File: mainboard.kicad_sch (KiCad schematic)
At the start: 30 parts, among them J1 terminal_led-strip, J2 header_rotary-encoder, J3 AudioJack2, J4 header_rpi, J5 power_input, Q1 IRF9540N, SW1 power_switch, U2 MSGEQ7, U3 OPA197xDBV, U4 logic-level-converter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

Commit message: finish schematic
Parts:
- removed R_led-strip_1, R_led-strip_2: 220, Resistor_SMD:R_0603_1608Metric_Pad0.98x0.95mm_HandSolder, symbol Device:R
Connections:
- net at R3.2, R5.1: now also U6.6 (4)
- net at U4.11 (HV2): now also J1.5 (Pin_5)
- net at U4.12 (HV1): now also J1.2 (Pin_2)
- net rotary_sw: now reaches J2.3 (Pin_3)
- net rotary_sw: now also U6.28 (1)
- net rotary_dt: now reaches J2.4 (Pin_4)
- net rotary_dt: now also U6.27 (2)
- net rotary_clk: now reaches J2.5 (Pin_5)
- net rotary_clk: now also U6.26 (3)
- net at J4.2 (Pin_2), SCL_pullup.2: now also U6.22 (RX)
- net at J4.3 (Pin_3), SDA_pullup.2: now also U6.21 (TX)
- net esp_led-strip_back: now reaches U6.12 (9)
- net esp_led-strip_back: now also U4.2 (LV2)
- net at U6.24 (10): now also U5.1 (LV1)
- net esp_msgeq7-strobe: now reaches U6.7 (5)
- net esp_msgeq7-strobe: now also U4.5 (LV3)
- net esp_msgeq7-reset: now reaches U6.8 (6)
- net esp_msgeq7-reset: now also U4.6 (LV4)
- net esp_led-strip_front: now reaches U6.9 (7)
- net esp_led-strip_front: now also U4.1 (LV1)
- net msgeq7_out renamed msgeq7-out
- net msgeq7_reset renamed msgeq7-reset
- net msgeq7_strobe renamed msgeq7-strobe
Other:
- moved on the sheet: U5

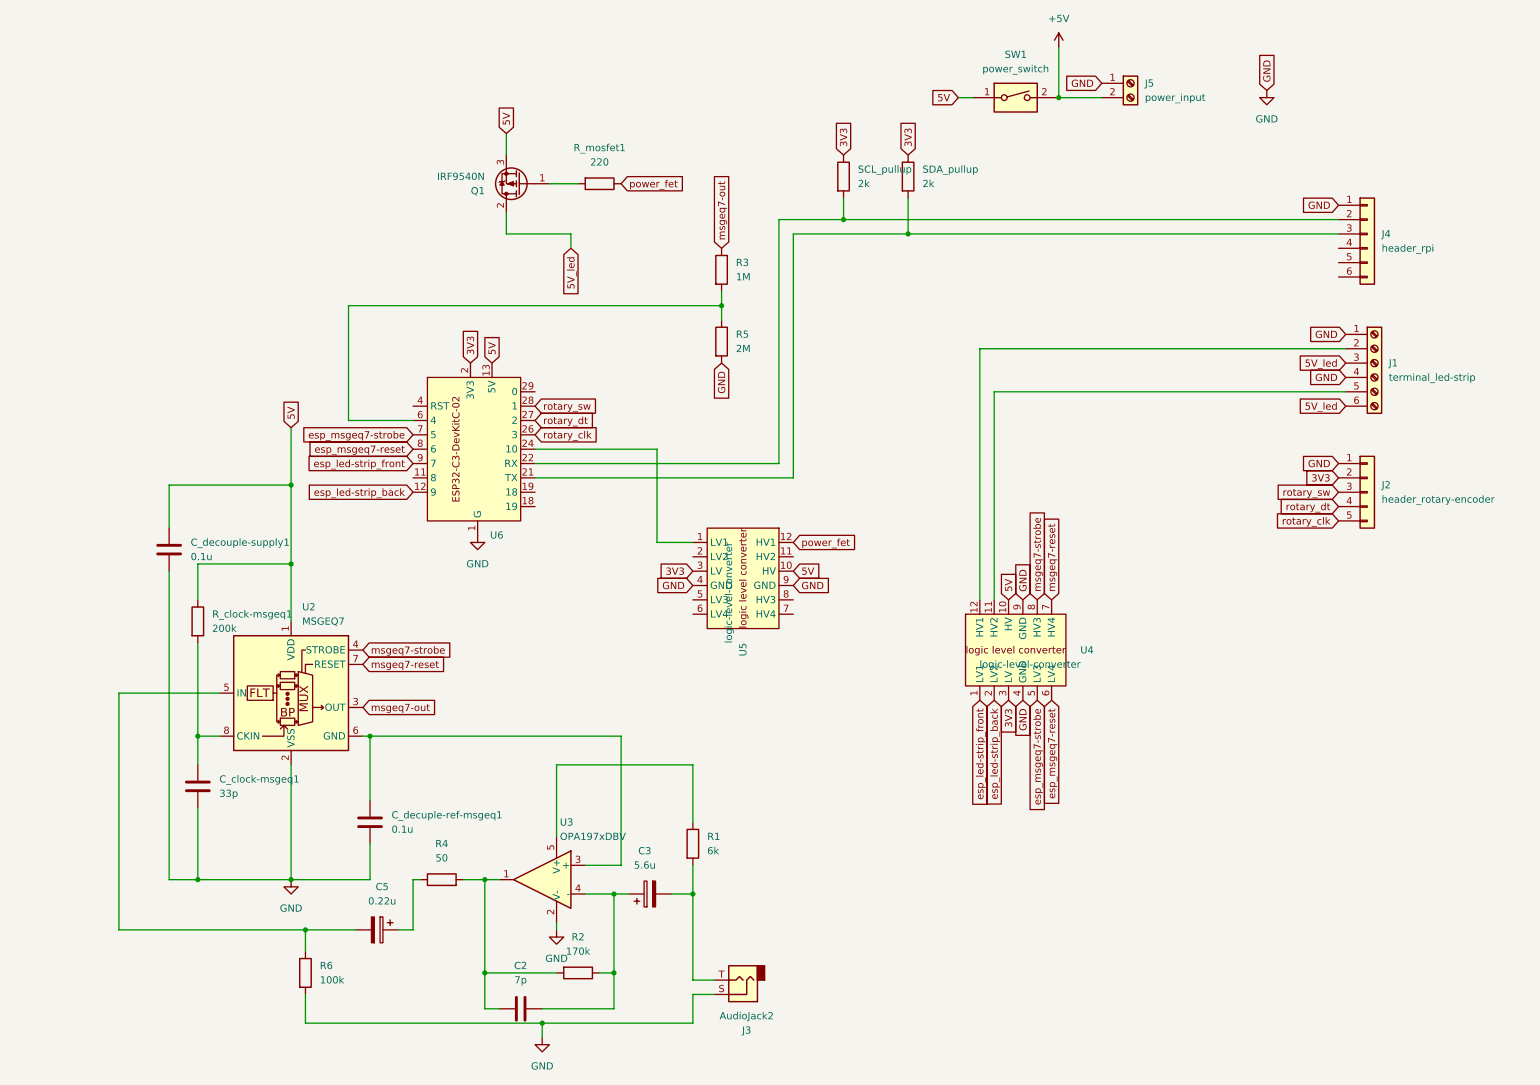
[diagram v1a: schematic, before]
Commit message: move i2c pins
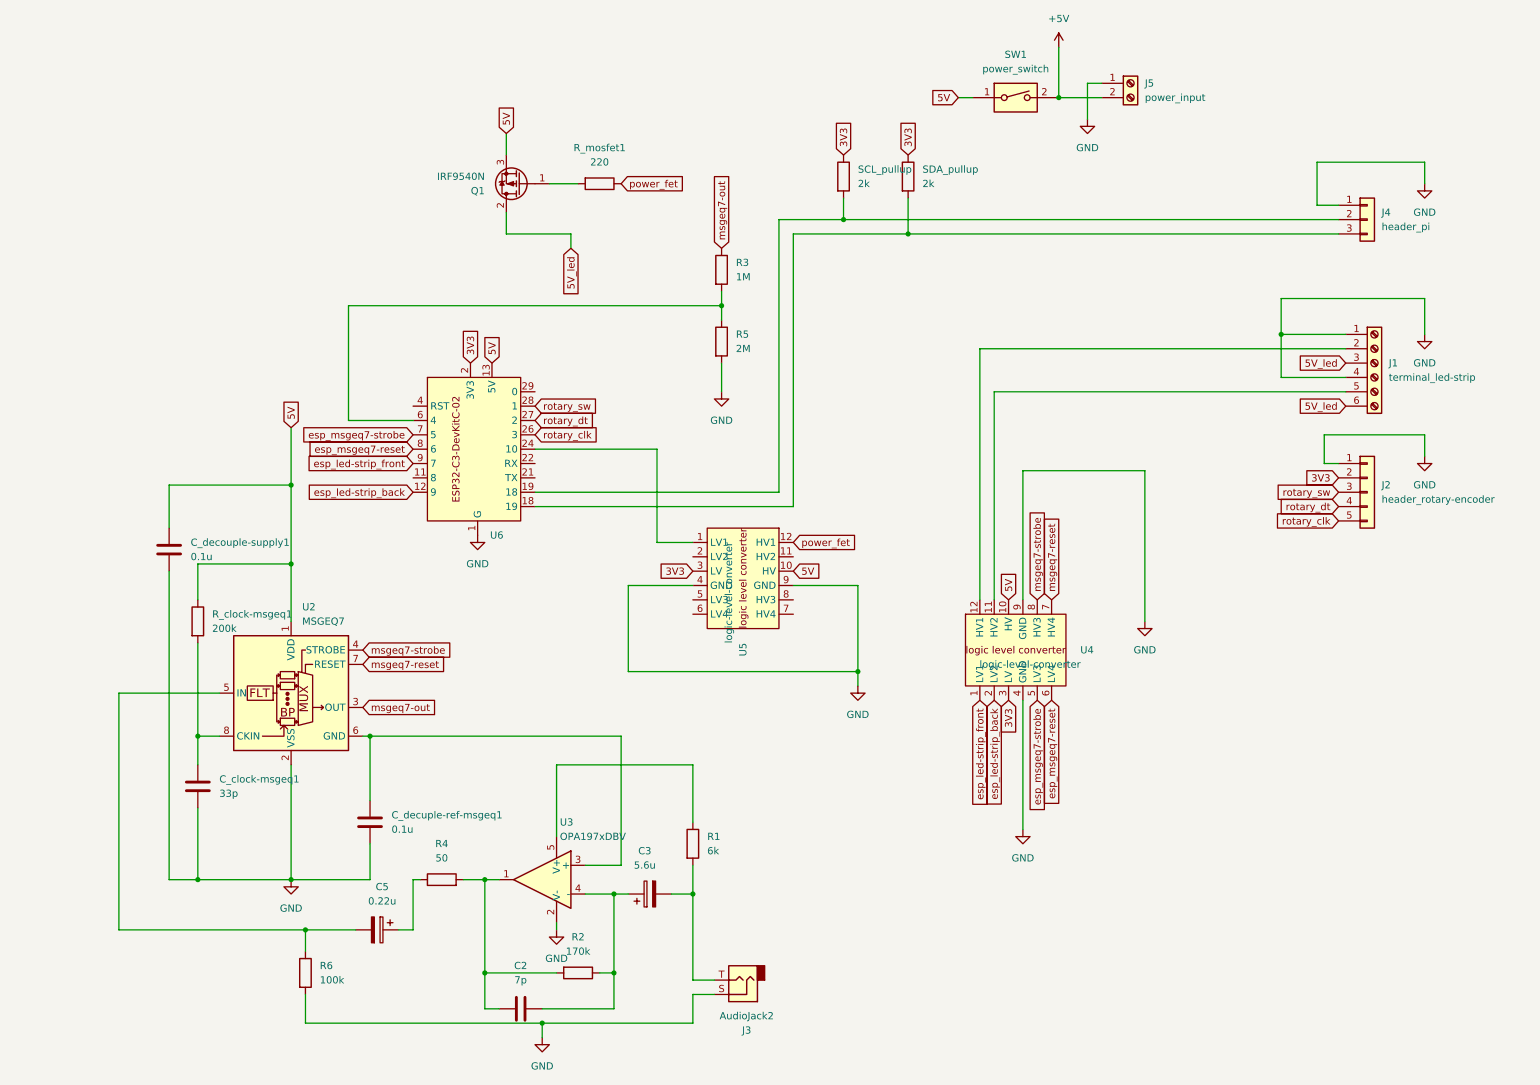
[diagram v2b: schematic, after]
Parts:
- removed J4: header_rpi, Connector_PinHeader_2.54mm:PinHeader_1x06_P2.54mm_Vertical, symbol Connector_Generic:Conn_01x06
- added J4: header_pi, symbol Connector_Generic:Conn_01x03
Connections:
- net GND: now also J4.1 (Pin_1)
- net at SCL_pullup.2: now also U6.19 (18), J4.2 (Pin_2); no longer U6.22 (RX)
- net at SDA_pullup.2: now also U6.18 (19), J4.3 (Pin_3); no longer U6.21 (TX)

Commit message: add loudness control
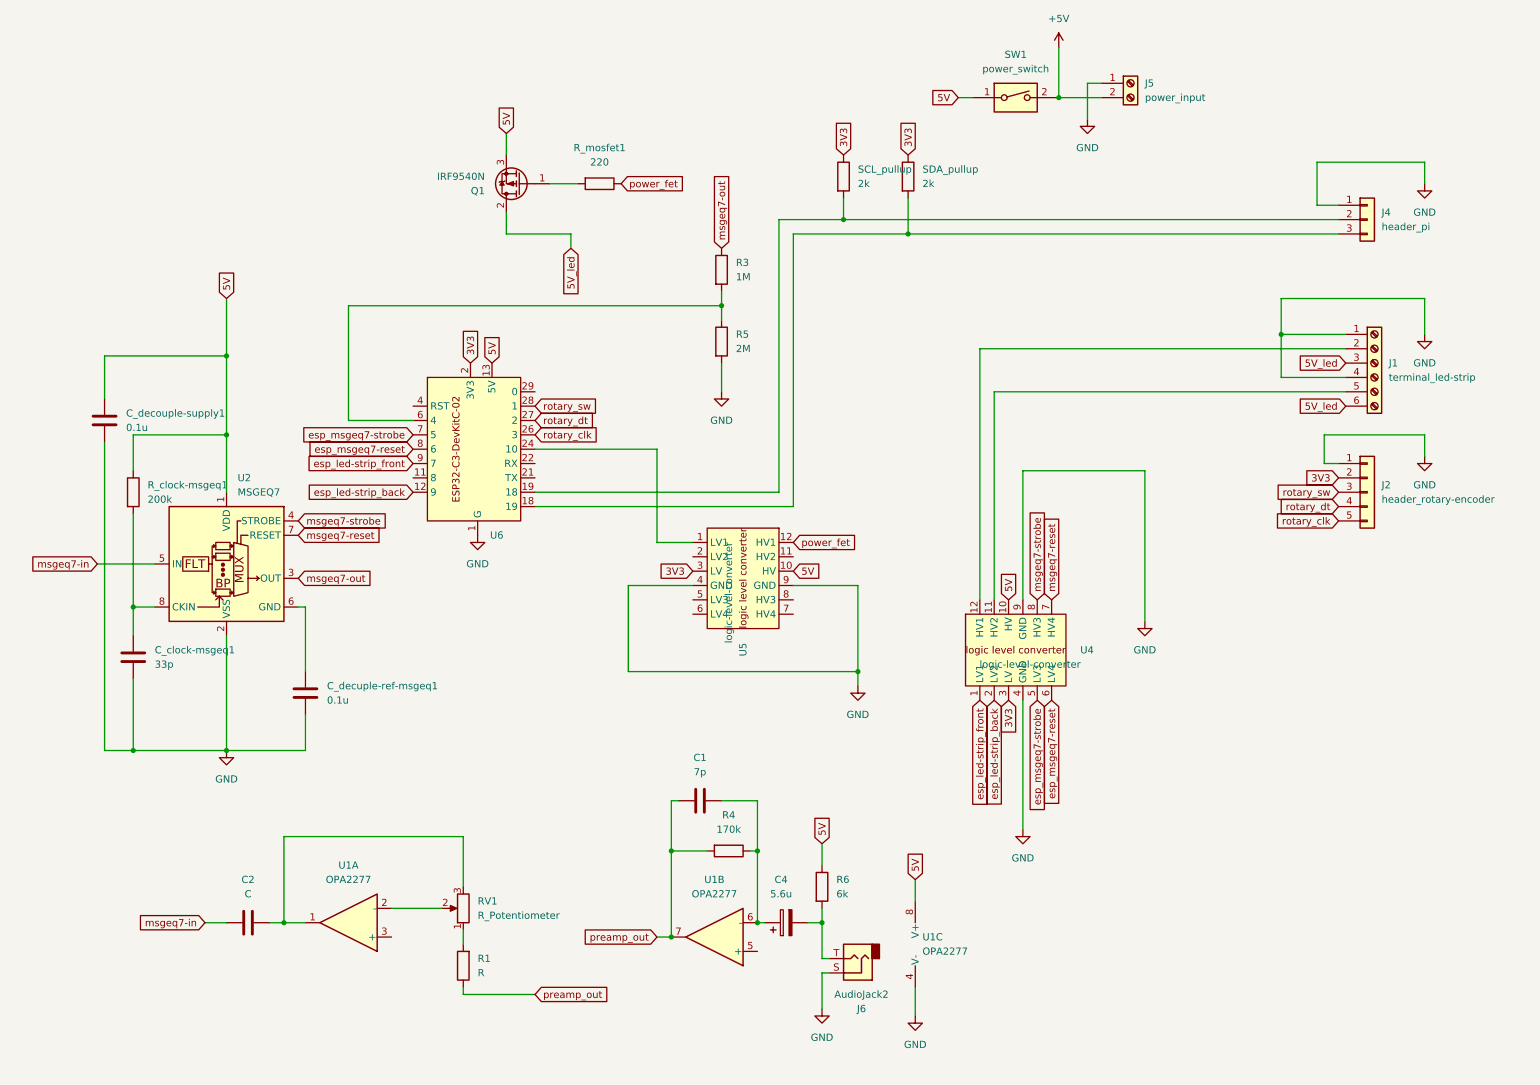
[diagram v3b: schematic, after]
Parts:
- removed C3: 5.6u, Capacitor_Tantalum_SMD:CP_EIA-7343-31_Kemet-D_Pad2.25x2.55mm_HandSolder, symbol Device:C_Polarized
- removed C5: 0.22u, Capacitor_Tantalum_SMD:CP_EIA-3216-18_Kemet-A_Pad1.58x1.35mm_HandSolder, symbol Device:C_Polarized
- removed J3: AudioJack2, my_lib:jack_3.5mm_TS-only, symbol Connector_Audio:AudioJack2
- removed R2: 170k, Resistor_SMD:R_0603_1608Metric_Pad0.98x0.95mm_HandSolder, symbol Device:R
- removed U3: OPA197xDBV, Package_TO_SOT_SMD:SOT-23-5, symbol Amplifier_Operational:OPA197xDBV
- added C1: 7p, Capacitor_SMD:C_0603_1608Metric_Pad1.08x0.95mm_HandSolder, symbol Device:C
- added C4: 5.6u, Capacitor_Tantalum_SMD:CP_EIA-7343-31_Kemet-D_Pad2.25x2.55mm_HandSolder, symbol Device:C_Polarized
- added J6: AudioJack2, my_lib:jack_3.5mm_TS-only, symbol Connector_Audio:AudioJack2
- added RV1: R_Potentiometer, symbol Device:R_Potentiometer
- added U1: OPA2277, Package_DIP:DIP-8_W7.62mm_Socket, symbol Amplifier_Operational:OPA2277
- C2: value 7p -> C; footprint Capacitor_SMD:C_0603_1608Metric_Pad1.08x0.95mm_HandSolder -> (none)
- R1: value 6k -> R; footprint Resistor_SMD:R_0603_1608Metric_Pad0.98x0.95mm_HandSolder -> (none)
- R4: value 50 -> 170k
- R6: value 100k -> 6k
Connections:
- net 5V: now also R6.1, U1.8 (V+)
- net GND: now also J6.S, U1.4 (V-); no longer R6.2
- net at C2.2: now also RV1.3, U1.1
- net at R1.2: now also RV1.1
- net at R4.1: now also C1.2, C4.1, U1.6 (-)
- net msgeq7-in: now reaches U2.5 (IN)
- net msgeq7-in: now also C2.1; no longer R6.1
- net preamp_out: now reaches R4.2
- net preamp_out: now also R1.1, C1.1, U1.7; no longer C2.1
- new net: C4.2, J6.T, R6.2
- new net: RV1.2, U1.2 (-)
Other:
- moved on the sheet: C_clock-msgeq1, C_decouple-supply1, C_decuple-ref-msgeq1, R_clock-msgeq1, U2
